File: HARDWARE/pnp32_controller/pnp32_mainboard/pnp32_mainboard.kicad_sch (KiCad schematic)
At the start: 8 parts

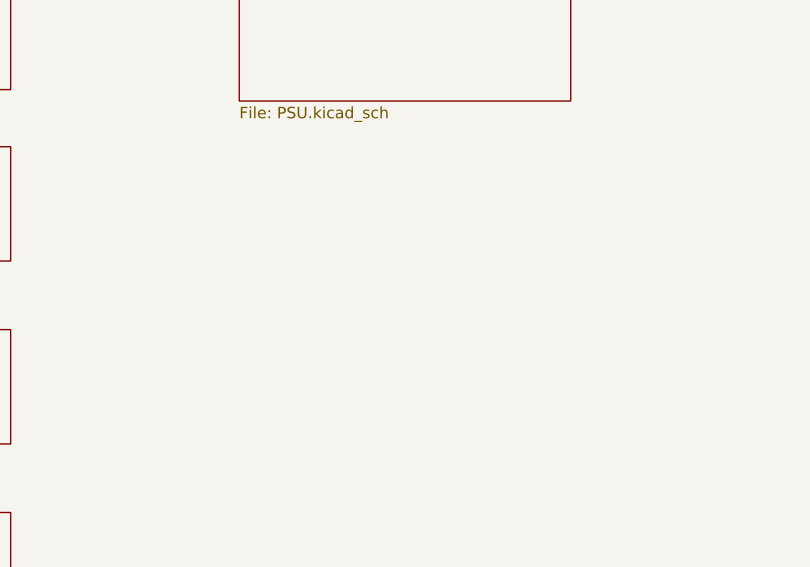
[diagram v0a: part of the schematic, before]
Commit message: update_PSU
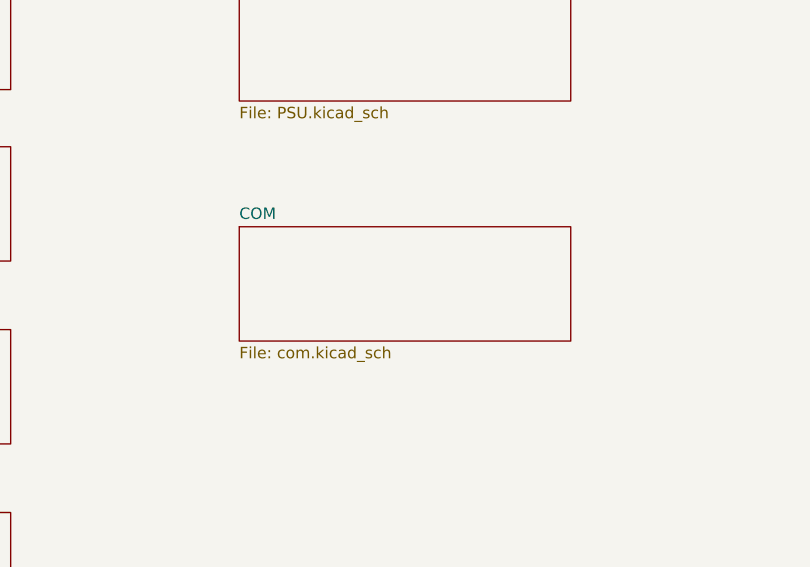
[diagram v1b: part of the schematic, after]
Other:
- added sheet COM (com.kicad_sch)
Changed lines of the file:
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@@
 		(dnp no)
 		(fields_autoplaced yes)
-		(property "Reference" "#PWR0164"
+		(property "Reference" "#PWR01"
 			(at 154.94 195.58 0)
 			(effects
@@
 			(project "pnp32_mainboard"
 				(path "/a02e5dd1-80da-4253-b87a-c8707aa3e0b0"
-					(reference "#PWR0164")
+					(reference "#PWR01")
 					(unit 1)
 				)
@@
 			(project "pnp32_mainboard"
 				(path "/a02e5dd1-80da-4253-b87a-c8707aa3e0b0"
-					(page "8")
+					(page "9")
 				)
 			)
@@
 			(project "pnp32_mainboard"
 				(path "/a02e5dd1-80da-4253-b87a-c8707aa3e0b0"
-					(page "13")
+					(page "14")
 				)
 			)
@@
 			(project "pnp32_mainboard"
 				(path "/a02e5dd1-80da-4253-b87a-c8707aa3e0b0"
-					(page "6")
+					(page "7")
 				)
 			)
@@
 			(project "pnp32_mainboard"
 				(path "/a02e5dd1-80da-4253-b87a-c8707aa3e0b0"
-					(page "12")
+					(page "13")
 				)
 			)
@@
 			(project "pnp32_mainboard"
 				(path "/a02e5dd1-80da-4253-b87a-c8707aa3e0b0"
-					(page "17")
+					(page "18")
 				)
 			)
@@
 			(project "pnp32_mainboard"
 				(path "/a02e5dd1-80da-4253-b87a-c8707aa3e0b0"
-					(page "19")
+					(page "20")
+				)
+			)
+		)
+	)
+	(sheet
+		(at 156.21 124.46)
+		(size 36.83 12.7)
+		(exclude_from_sim no)
+		(in_bom yes)
+		(on_board yes)
+		(dnp no)
+		(fields_autoplaced yes)
+		(stroke
+			(width 0.1524)
+			(type solid)
+		)
+		(fill
+			(color 0 0 0 0.0000)
+		)
+		(property "Sheetname" "COM"
+			(at 156.21 123.7484 0)
+			(effects
+				(font
+					(size 1.27 1.27)
+				)
+				(justify left bottom)
+			)
+		)
+		(property "Sheetfile" "com.kicad_sch"
+			(at 156.21 137.7446 0)
+			(effects
+				(font
+					(size 1.27 1.27)
+				)
+				(justify left top)
+			)
+		)
+		(instances
+			(project "pnp32_mainboard"
+				(path "/a02e5dd1-80da-4253-b87a-c8707aa3e0b0"
+					(page "3")
 				)
 			)
@@
 			(project "pnp32_mainboard"
 				(path "/a02e5dd1-80da-4253-b87a-c8707aa3e0b0"
-					(page "4")
+					(page "5")
 				)
 			)
@@
 			(project "pnp32_mainboard"
 				(path "/a02e5dd1-80da-4253-b87a-c8707aa3e0b0"
-					(page "9")
+					(page "10")
 				)
 			)
@@
 			(project "pnp32_mainboard"
 				(path "/a02e5dd1-80da-4253-b87a-c8707aa3e0b0"
-					(page "21")
+					(page "22")
 				)
 			)
@@
 			(project "pnp32_mainboard"
 				(path "/a02e5dd1-80da-4253-b87a-c8707aa3e0b0"
-					(page "15")
+					(page "16")
 				)
 			)
@@
 			(project "pnp32_mainboard"
 				(path "/a02e5dd1-80da-4253-b87a-c8707aa3e0b0"
-					(page "11")
+					(page "12")
 				)
 			)
@@
 			(project "pnp32_mainboard"
 				(path "/a02e5dd1-80da-4253-b87a-c8707aa3e0b0"
-					(page "18")
+					(page "19")
 				)
 			)
@@
 			(project "pnp32_mainboard"
 				(path "/a02e5dd1-80da-4253-b87a-c8707aa3e0b0"
-					(page "22")
+					(page "23")
 				)
 			)
@@
 			(project "pnp32_mainboard"
 				(path "/a02e5dd1-80da-4253-b87a-c8707aa3e0b0"
-					(page "5")
+					(page "6")
 				)
 			)
@@
 			(project "pnp32_mainboard"
 				(path "/a02e5dd1-80da-4253-b87a-c8707aa3e0b0"
-					(page "20")
+					(page "21")
 				)
 			)
@@
 			(project "pnp32_mainboard"
 				(path "/a02e5dd1-80da-4253-b87a-c8707aa3e0b0"
-					(page "7")
+					(page "8")
 				)
 			)
@@
 			(project "pnp32_mainboard"
 				(path "/a02e5dd1-80da-4253-b87a-c8707aa3e0b0"
-					(page "16")
+					(page "17")
 				)
 			)
@@
 			(project "pnp32_mainboard"
 				(path "/a02e5dd1-80da-4253-b87a-c8707aa3e0b0"
-					(page "14")
+					(page "15")
 				)
 			)
@@
 			(project "pnp32_mainboard"
 				(path "/a02e5dd1-80da-4253-b87a-c8707aa3e0b0"
-					(page "3")
+					(page "4")
 				)
 			)
@@
 			(project "pnp32_mainboard"
 				(path "/a02e5dd1-80da-4253-b87a-c8707aa3e0b0"
-					(page "10")
-				)
-			)
+					(page "11")
+				)
+			)
